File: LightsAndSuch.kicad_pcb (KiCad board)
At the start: 2 copper layers, 62 parts, among them J1 Conn_ARM_SWD_TagConnect_TC2030, Q1 AO3400A, Q2 AO3400A, Q3 AO3400A, U1 STM32F205RBTx, U2 MAX98357A, U3 TPS54202DDC, U4 TPS7A20xxxDQN, U5 CD4081BM, U6 LM555xM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

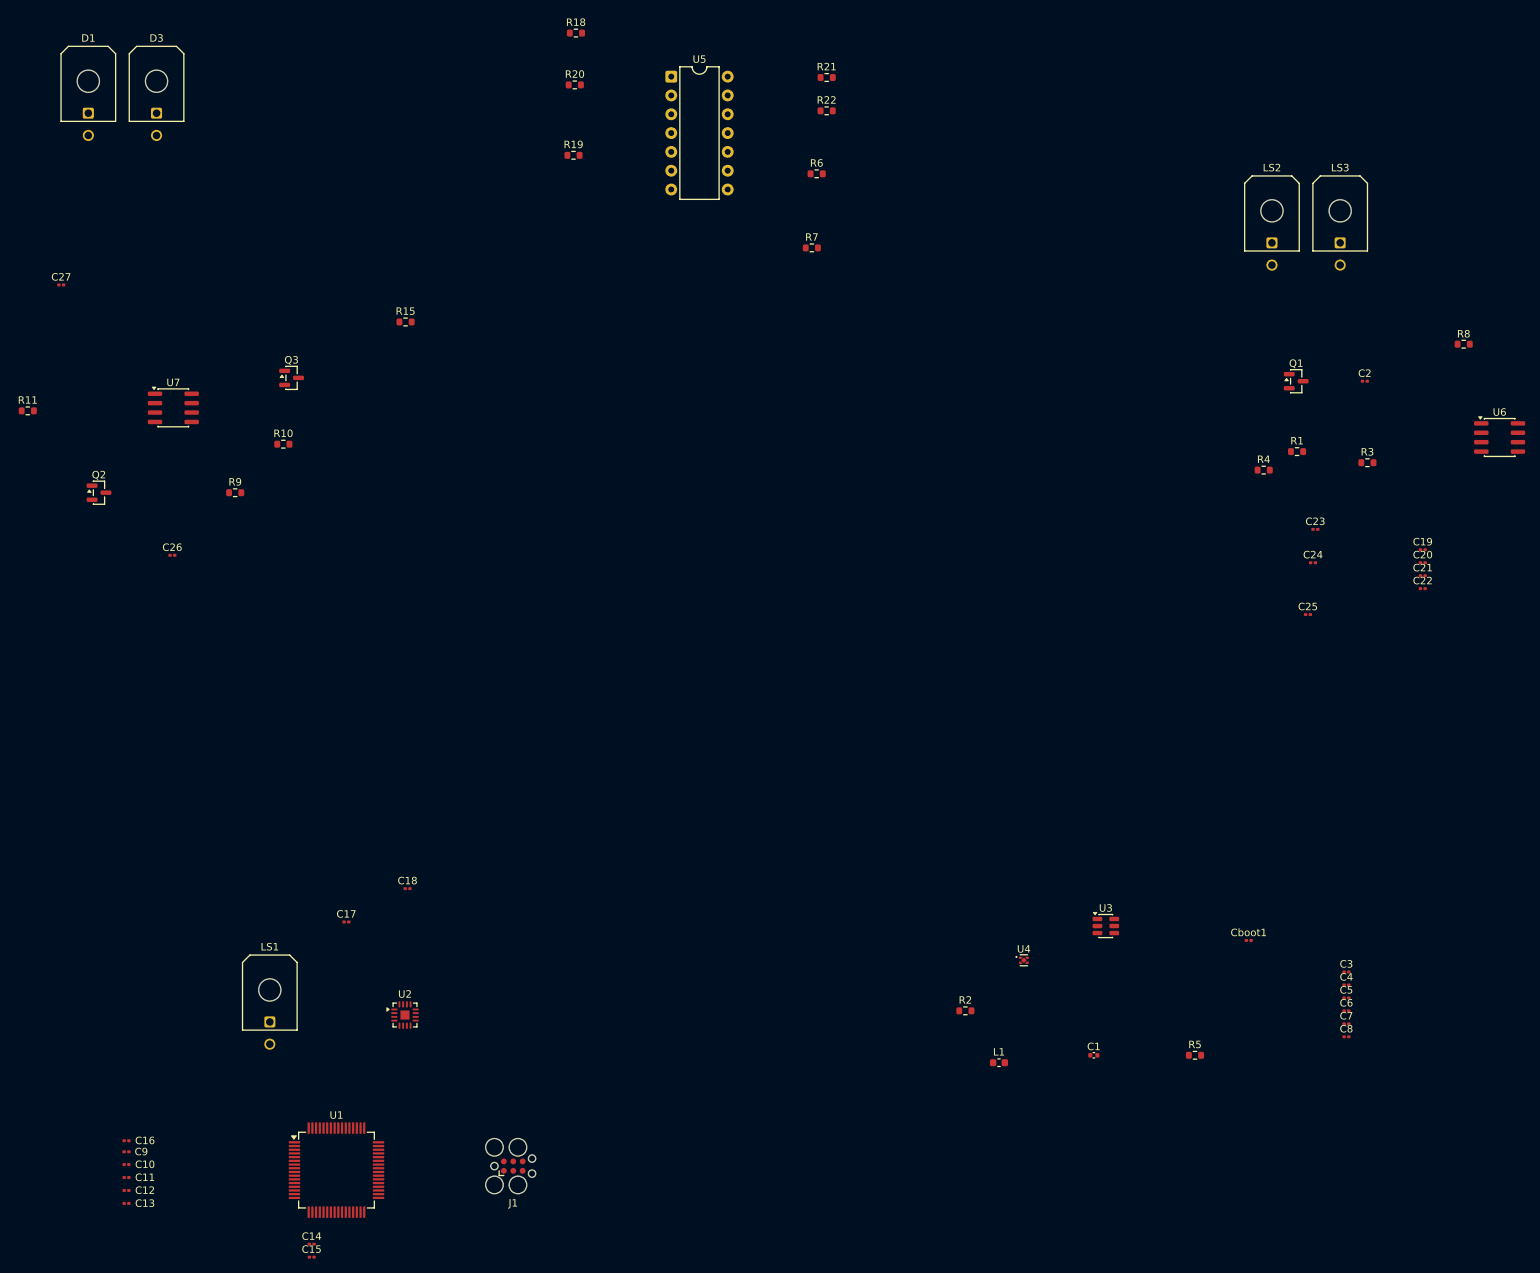
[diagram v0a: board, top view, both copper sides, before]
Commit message: ground plane and cutouts
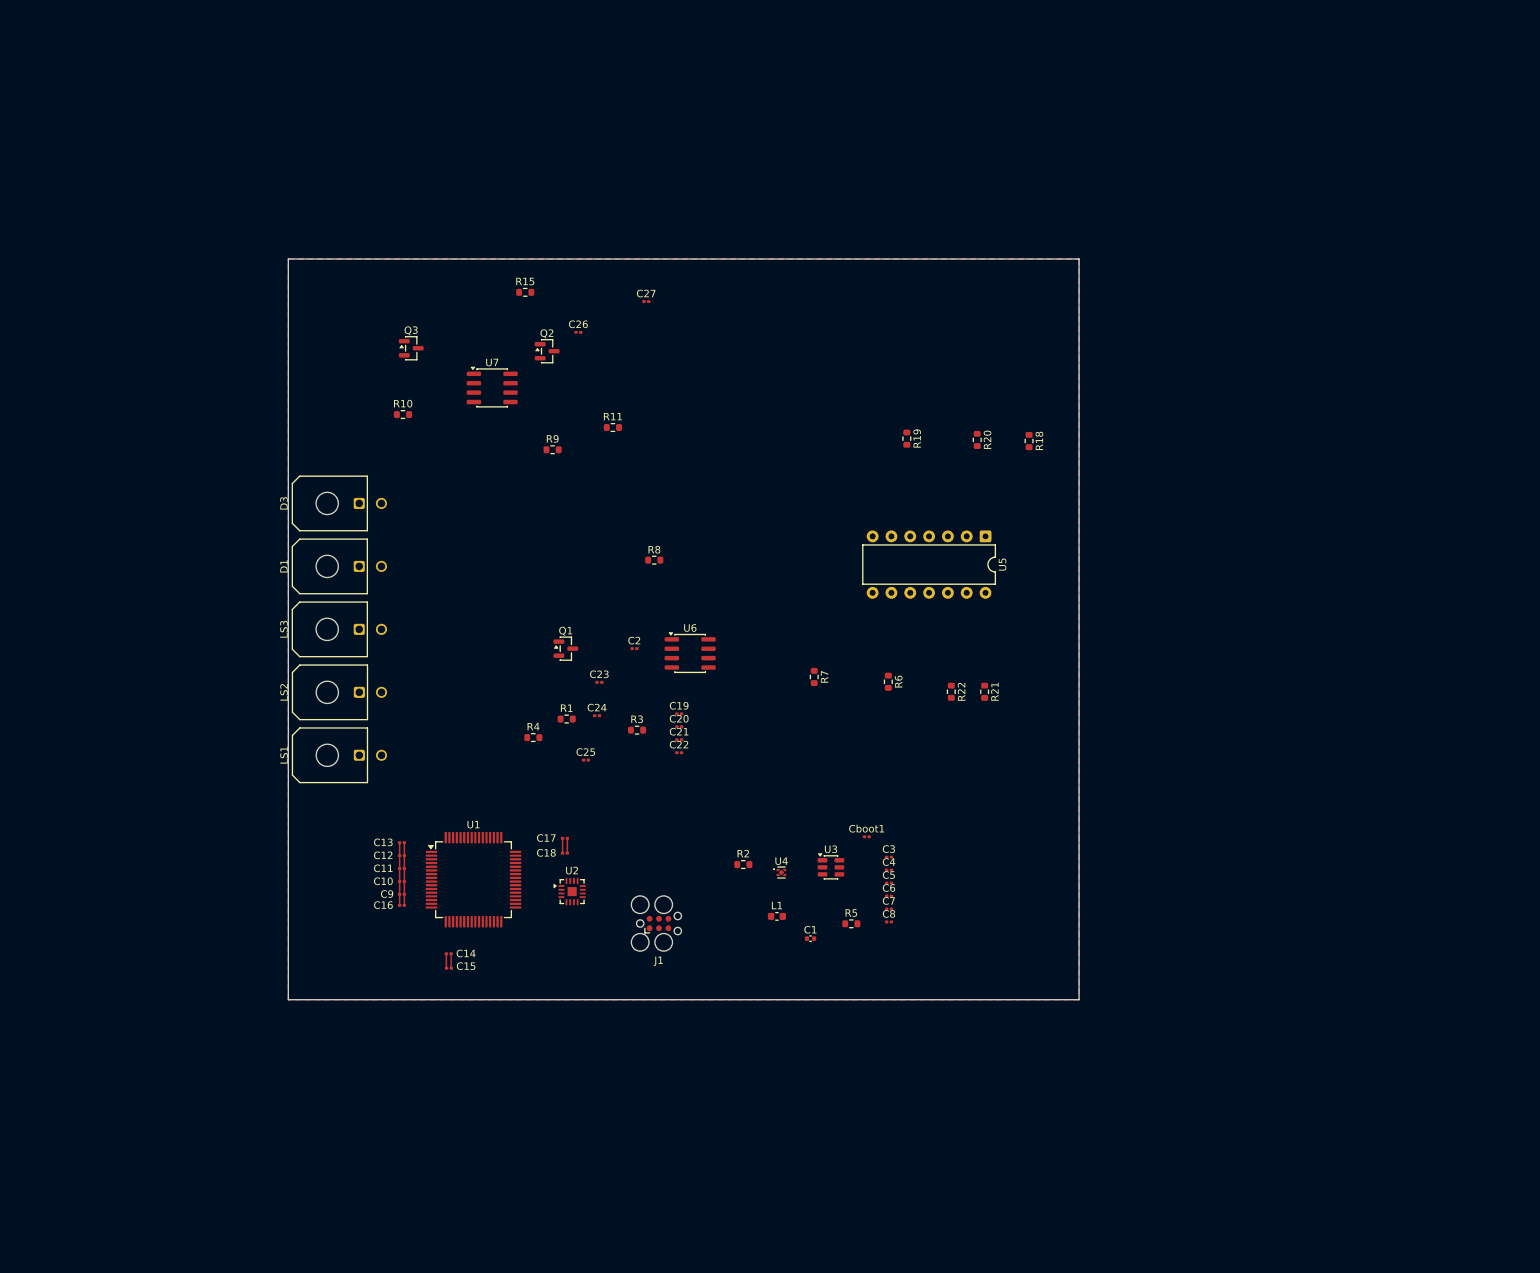
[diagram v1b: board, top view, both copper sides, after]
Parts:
- moved LS3 142.3 mm to (67.1, 97.0), turned to 90 degrees
- moved LS2 137.3 mm to (67.1, 105.5), turned to 90 degrees
- moved R8 113.1 mm to (106.9, 87.7)
- moved U6 113.1 mm to (111.8, 100.2)
- moved C2 105.0 mm to (104.2, 99.6)
- moved R1 105.0 mm to (95.1, 109.1)
- moved R3 105.0 mm to (104.6, 110.6)
- moved R4 105.0 mm to (90.6, 111.6)
- moved Q1 105.0 mm to (95.0, 99.6)
- moved C19 102.8 mm to (110.3, 108.4)
- moved C20 102.8 mm to (110.3, 110.2)
- moved C21 102.8 mm to (110.3, 111.9)
- moved C22 102.8 mm to (110.3, 113.7)
- moved C25 99.4 mm to (97.7, 114.7)
- moved C23 98.8 mm to (99.5, 104.2)
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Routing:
- net GND: track 0.00 -> 12.2 mm
- net +3.3V: track 0.00 -> 10.2 mm
- net +5V: track 0.00 -> 2.00 mm
- added copper zone on F.Cu, net GND
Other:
- board outline added: 106.8 x 100 mm

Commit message: more or less finished with power
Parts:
- added J2: VIN, Connector_Molex:Molex_Micro-Fit_3.0_43045-0200_2x01_P3.00mm_Horizontal, F.Cu at (154.7, 116.0)
- added J3: TSA, Connector_Molex:Molex_Micro-Fit_3.0_43045-0200_2x01_P3.00mm_Horizontal, F.Cu at (154.8, 88.9)
- added J4: BMS Fault, Connector_Molex:Molex_Micro-Fit_3.0_43045-0200_2x01_P3.00mm_Horizontal, F.Cu at (154.8, 98.1)
- added J5: Button, Connector_Molex:Molex_Micro-Fit_3.0_43045-0200_2x01_P3.00mm_Horizontal, F.Cu at (154.8, 107.3)
- added J6: IMD Fault, Connector_Molex:Molex_Micro-Fit_3.0_43045-0200_2x01_P3.00mm_Horizontal, F.Cu at (154.7, 80.2)
- added J7: Break, Connector_Molex:Molex_Micro-Fit_3.0_43045-0200_2x01_P3.00mm_Horizontal, F.Cu at (154.7, 72.0)
- U4: value TPS7A20xxxDQN -> PTPS7A20185PDQNR; footprint Package_SON:Texas_X2SON-4_1x1mm_P0.65mm -> PTPS7A20185PDQNR:DQN0004A-MFG
- moved C1 29.5 mm to (149.4, 118.4), turned to -90 degrees
- moved L1 24.8 mm to (144.6, 122.8), turned to 180 degrees
- moved R18 23.8 mm to (145.8, 50.9)
- moved R19 23.8 mm to (129.2, 50.6)
- moved R20 23.8 mm to (138.8, 50.8)
- moved R21 23.8 mm to (139.8, 84.8)
- moved R22 23.8 mm to (135.2, 84.8)
- moved R6 23.8 mm to (126.8, 83.4)
- moved R7 23.8 mm to (116.8, 82.8)
- moved U5 23.8 mm to (139.9, 63.8)
- moved J1 20.4 mm to (87.2, 138.1)
- moved R2 20.1 mm to (136.3, 118.8), turned to 90 degrees
- moved R5 18.9 mm to (139.2, 118.8), turned to -90 degrees
- moved U4 17.3 mm to (140.5, 124.4), turned to 90 degrees
- moved U3 15.8 mm to (142.9, 119.0), turned to 180 degrees
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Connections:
- net Net-(U3-SW) renamed /SW
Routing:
- net +3.3V: track 10.2 -> 0.00 mm
- net Net-(U3-FB): track 0.00 -> 8.60 mm
- net GND: track 12.2 -> 5.40 mm, vias 0 -> 6
- net Net-(U3-BOOT): track 0.00 -> 4.49 mm
- added copper zone on F.Cu, net +12V
- added copper zone on F.Cu, net +5V
- added copper zone on F.Cu, net /SW
- added copper zone on B.Cu, net GND
- removed copper zone on F.Cu, net GND
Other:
- board size 106.8 x 100 mm -> 106.7 x 100 mm

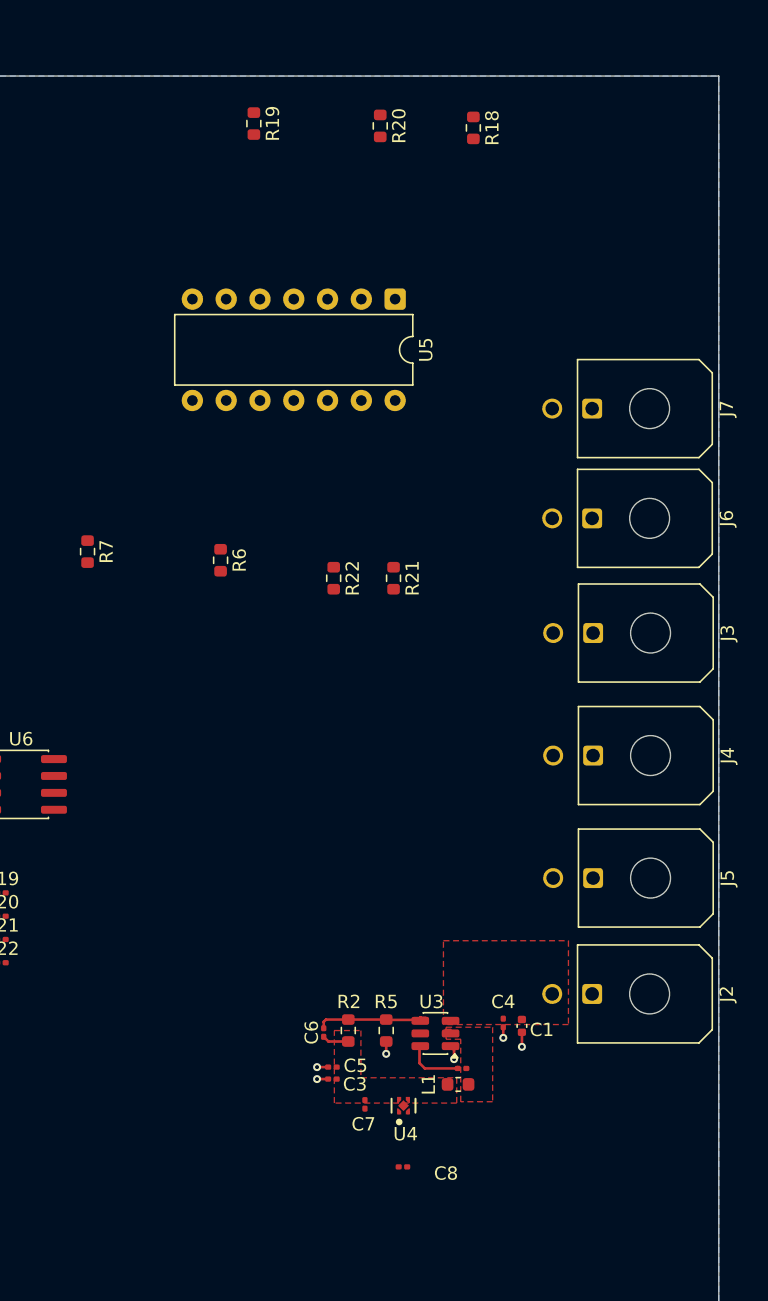
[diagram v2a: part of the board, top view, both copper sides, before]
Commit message: finished power layout + inverted sig
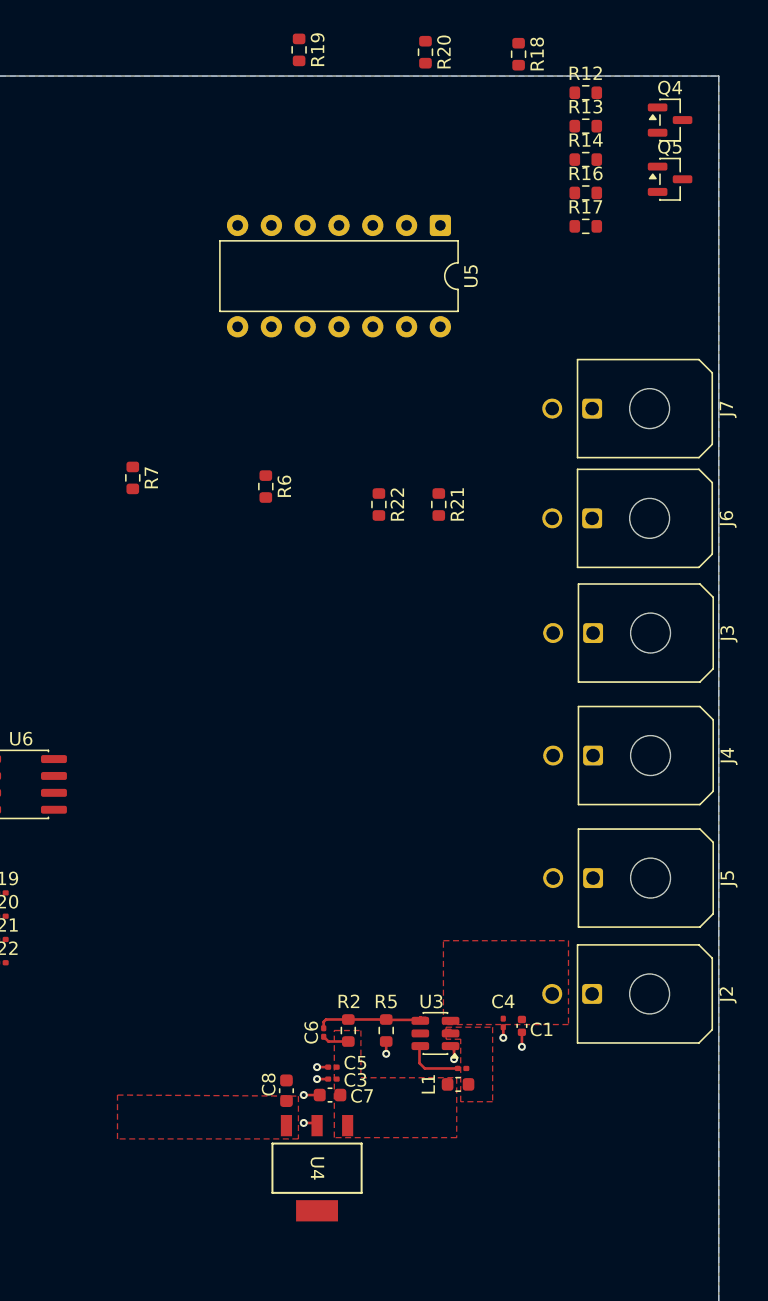
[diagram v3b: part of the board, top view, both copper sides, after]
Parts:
- added Q4: AO3400A, Package_TO_SOT_SMD:SOT-23, F.Cu at (160.5, 50.3)
- added Q5: AO3400A, Package_TO_SOT_SMD:SOT-23, F.Cu at (160.5, 54.8)
- added R12: 10k, Resistor_SMD:R_0603_1608Metric, F.Cu at (154.2, 48.3)
- added R13: 5k, Resistor_SMD:R_0603_1608Metric, F.Cu at (154.2, 50.8)
- added R14: 10k, Resistor_SMD:R_0603_1608Metric, F.Cu at (154.2, 53.3)
- added R16: 10k, Resistor_SMD:R_0603_1608Metric, F.Cu at (154.2, 55.8)
- added R17: 5k, Resistor_SMD:R_0603_1608Metric, F.Cu at (154.2, 58.3)
- C7: value 1u -> 0.47u; footprint Capacitor_SMD:C_0201_0603Metric -> Capacitor_SMD:C_0603_1608Metric
- C8: value 1u -> 33u; footprint Capacitor_SMD:C_0201_0603Metric -> Capacitor_SMD:C_0603_1608Metric
- U4: value PTPS7A20185PDQNR -> LM3940IMP-3.3; footprint PTPS7A20185PDQNR:DQN0004A-MFG -> LM3940:MP04A
- moved C8 10.5 mm to (131.7, 123.3), turned to 90 degrees
- moved U4 8.02 mm to (134.0, 129.1), turned to 180 degrees
- moved R19 6.50 mm to (132.7, 45.0)
- moved R21 6.50 mm to (143.2, 79.2)
- moved R22 6.50 mm to (138.7, 79.2)
- moved R6 6.50 mm to (130.2, 77.9)
- moved R7 6.50 mm to (120.2, 77.2)
- moved U5 6.50 mm to (143.3, 58.2)
- moved R18 6.50 mm to (149.2, 45.4)
- moved R20 6.50 mm to (142.2, 45.2)
- moved C7 2.72 mm to (135.0, 123.6), turned to 180 degrees
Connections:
- D3 pad 2: Net-(D3-A) -> +12V
- Q3 pad 3: Net-(D3-A) -> +12V
- R21 pad 1: BMS_Fault -> IMD_Fault
- R21 pad 2: GND -> Net-(Q5-G)
- U4 pad 1: +3.3V -> +5V
- U4 pad 3: +5V -> +3.3V
- U5 pad 12: IMD_Fault -> Net-(Q5-D)
- U5 pad 13: BMS_Fault -> Net-(Q4-D)
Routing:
- net GND: track 5.40 -> 7.69 mm, vias 6 -> 8
- added copper zone on F.Cu, net +3.3V

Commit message: I/O stuff
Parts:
- removed R22: 10k, Resistor_SMD:R_0603_1608Metric
- moved Q5 58.3 mm to (143.9, 110.7)
- moved R16 57.9 mm to (145.7, 113.0), turned to 90 degrees
- moved Q4 54.2 mm to (143.4, 101.7), turned to -90 degrees
- moved R12 51.0 mm to (146.9, 98.7), turned to 180 degrees
- moved R14 50.7 mm to (146.4, 103.4), turned to 180 degrees
- moved R17 50.1 mm to (143.7, 107.3), turned to 180 degrees
- moved R13 49.2 mm to (143.3, 98.7), turned to 180 degrees
- moved U5 48.4 mm to (138.8, 106.4)
- moved R18 44.8 mm to (146.2, 90.1), turned to 0 degrees
- moved R19 39.1 mm to (146.6, 81.6), turned to 0 degrees
- moved J5 34.5 mm to (152.7, 72.9)
- moved C19 31.7 mm to (92.8, 82.0)
- moved C20 31.7 mm to (92.8, 83.7)
- moved C21 31.7 mm to (92.8, 85.5)
- moved C22 31.7 mm to (92.8, 87.2)
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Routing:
- net Button: track 0.00 -> 44.6 mm
- net Break: track 0.00 -> 32.1 mm
- net TSA: track 0.00 -> 22.7 mm
- net Net-(Q4-D): track 0.00 -> 17.1 mm
- net Net-(Q5-D): track 0.00 -> 15.6 mm
- net +12V: track 0.00 -> 12.0 mm
- net GND: track 7.69 -> 14.2 mm, vias 8 -> 15
- net Net-(Q5-G): track 0.00 -> 5.00 mm
- net Net-(Q4-G): track 0.00 -> 4.08 mm
- net IMD_Fault: track 0.00 -> 2.15 mm
- net BMS_Fault: track 0.00 -> 2.08 mm
